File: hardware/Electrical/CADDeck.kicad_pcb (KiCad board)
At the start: 2 copper layers, 129 x 82.1 mm, 42 parts, among them J1 Conn_01x05_Socket, J4 Conn_01x04_Socket, J5 Conn_01x10_Socket, Q1 2N2222, SW1 SW_Push, SW10 SW_Push, SW2 SW_Push, SW3 SW_Push, SW4 SW_Push, SW5 SW_Push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

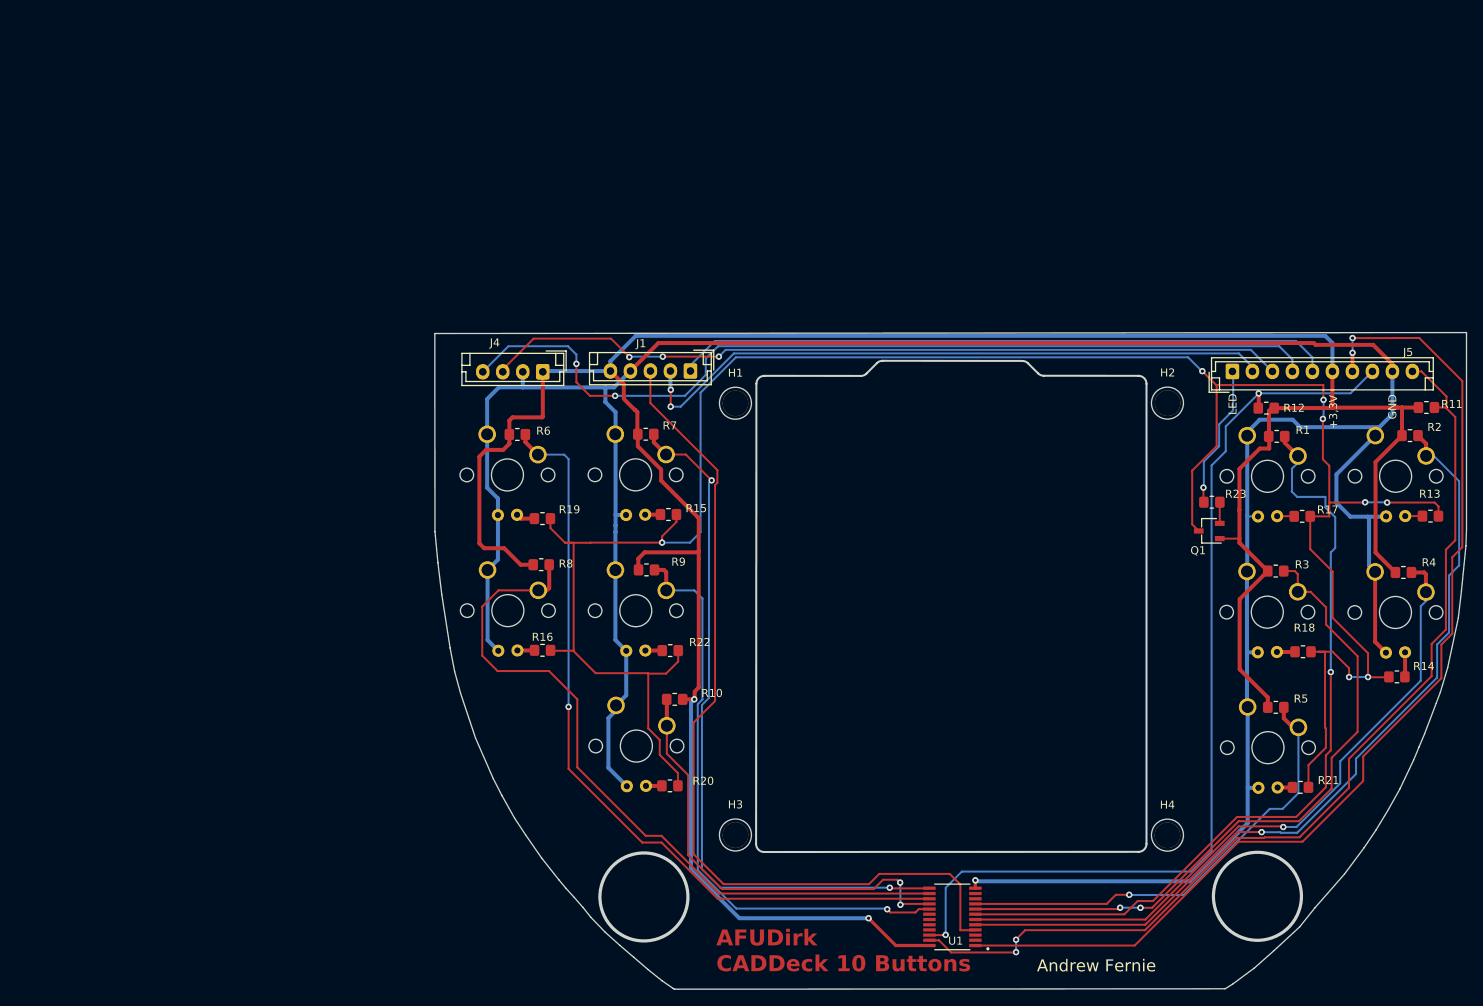
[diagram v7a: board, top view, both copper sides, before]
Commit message: Platinen optimiert
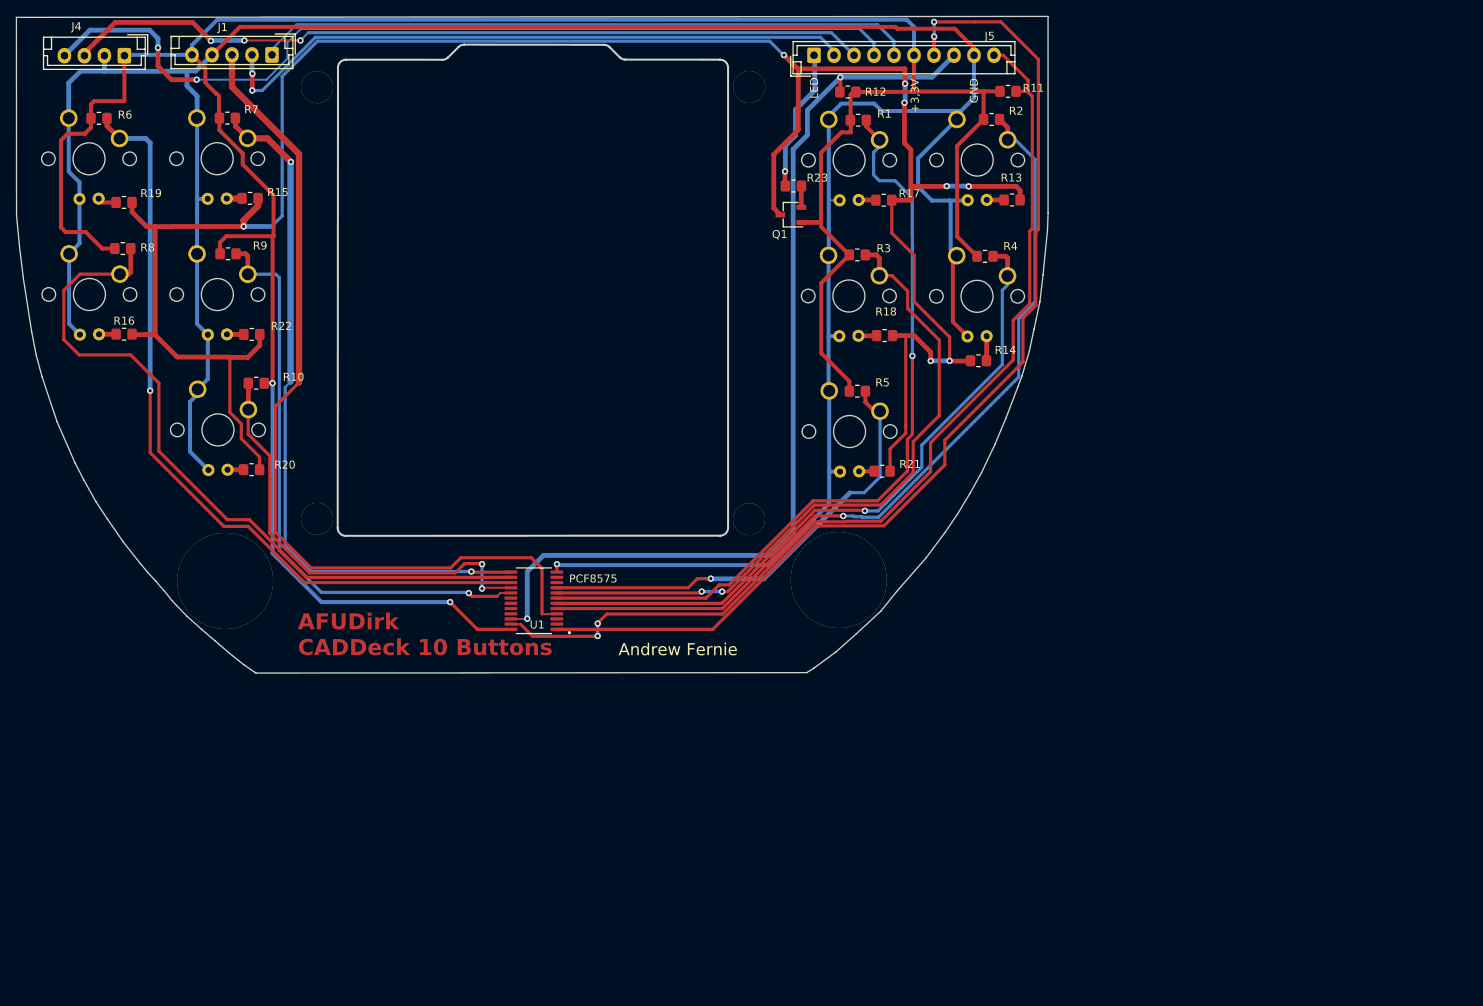
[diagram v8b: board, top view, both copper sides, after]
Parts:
- removed H1, H3, H4: Bohrung Joy, MountingHole:MountingHole_3.2mm_M3_DIN965
- added ?: , , F.Cu at (126.7, 80.0)
- added ?: , , F.Cu at (72.7, 79.9)
- added ?: , , F.Cu at (137.9, 87.6)
- added ?: , , F.Cu at (72.7, 26.0)
- added ?: , , F.Cu at (61.2, 87.7)
- moved R12 65.6 mm to (139.0, 26.6)
- moved R18 65.6 mm to (143.6, 57.0)
- moved R21 65.6 mm to (143.3, 74.0)
- moved R23 65.6 mm to (132.2, 38.3)
- moved R4 65.6 mm to (156.2, 47.1)
- moved SW2 65.6 mm to (152.7, 30.0)
- moved H2 65.6 mm to (126.7, 25.9)
- moved J1 65.6 mm to (67.0, 21.9)
- moved J4 65.6 mm to (48.6, 22.0)
- moved Q1 65.6 mm to (131.9, 41.9)
- moved R10 65.6 mm to (65.1, 63.0)
- moved R11 65.6 mm to (159.0, 26.5)
- moved R15 65.6 mm to (64.3, 39.9)
- moved R16 65.6 mm to (48.6, 56.8)
- moved R17 65.6 mm to (143.5, 40.1)
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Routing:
- net +3.3V: track 345.9 -> 344.0 mm
- net Net-(U1-P03): track 100.1 -> 98.7 mm
- net Net-(U1-P10): track 88.7 -> 87.6 mm
- net Net-(U1-P14): track 73.5 -> 72.8 mm
- net Net-(J5-Pin_10): track 124.4 -> 123.8 mm
- net Net-(J5-Pin_7): track 132.3 -> 131.7 mm
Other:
- outline, holes or cut-outs redrawn
- board text added: "PCF8575"
